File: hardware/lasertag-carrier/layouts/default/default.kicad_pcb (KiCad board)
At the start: 2 copper layers, 75 x 50 mm, 37 parts, among them J0 Power in 2P, J1 S3-Matrix L, J10 LS in, J11 LS out, J12 Ext button, J13 Touch hdr, J2 S3-Matrix R, J3 MAX98357A, J4 Speaker, J5 microSD, J6 IR RX, J7 IR LED, J8 WS2812 out, J9 OLED I2C, Q1 2N2222A, SW1 SW_PUSH_6mm, U1 74AHCT125

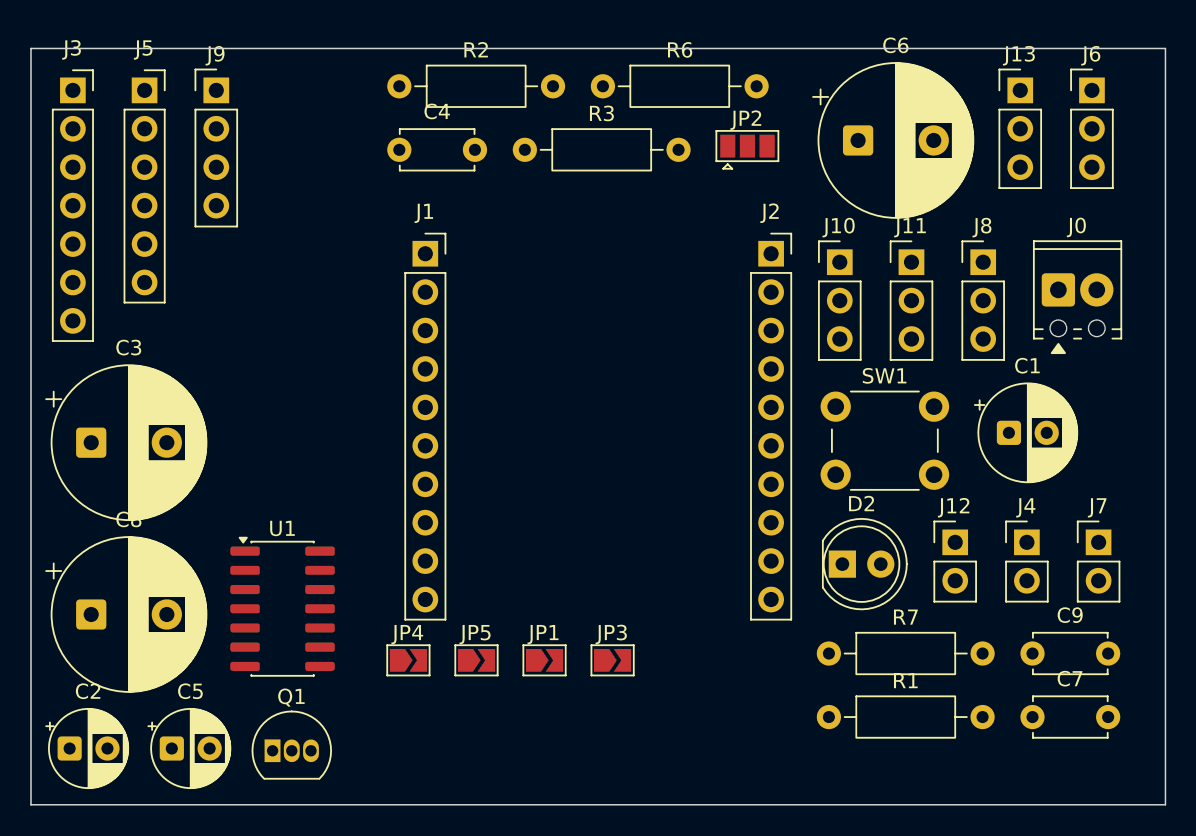
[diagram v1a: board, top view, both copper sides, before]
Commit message: Directed placement; drop level shifter from carrier; add activity-LED header
Floor plan per review: power (J0/C1/D2) bottom-left, audio (J3/C3/JP1/JP2/J4)
mid-left with the MAX98357A body reaching the left edge, microSD (J5/C4/C5/
JP3) bottom-right with the breakout body reaching the right edge, IR RX (J6/
C9) top-centre, IR TX driver (J7/Q1/R1/R2) top-right, GP2 role selector
bottom-centre, WS2812 out (J8/R3/C6) right edge.

- remove the 6 level-shifter parts (J10/J11/U1/R6/C7/C8) from the carrier:
  Block 7 is a standalone board per pcb-blocks.md; the ws-out header J8 stays
  as the cable output that will feed it if ring/status LEDs are added later
- add the activity-LED circuit the spec had deferred (Assumption #9): J14
  2-pin header at 25% from the left on the top edge + R9 220R series, wired
  GP7 (J1.4) -> R9 -> J14 -> GND to match the breadboard circuit the firmware
  already drives (activityLedPin = 7)
- keep main.ato in sync (documentation only -- do not rebuild with ato, the
  board file is the source of truth downstream of the keep-THT decision)
- regenerate bom.csv (33 parts)

Verified: no overlapping bounding boxes, nothing inside the module footprint
or under the elevated audio/microSD breakout bodies, zero DRC errors
(67 unconnected = ratsnest to route, plus cosmetic silk warnings).

Co-Authored-By: Claude Opus 4.8 <noreply@anthropic.com>
Claude-Session: https://claude.ai/code/session_01TutNLcDSScdeeVSbjpyg8j
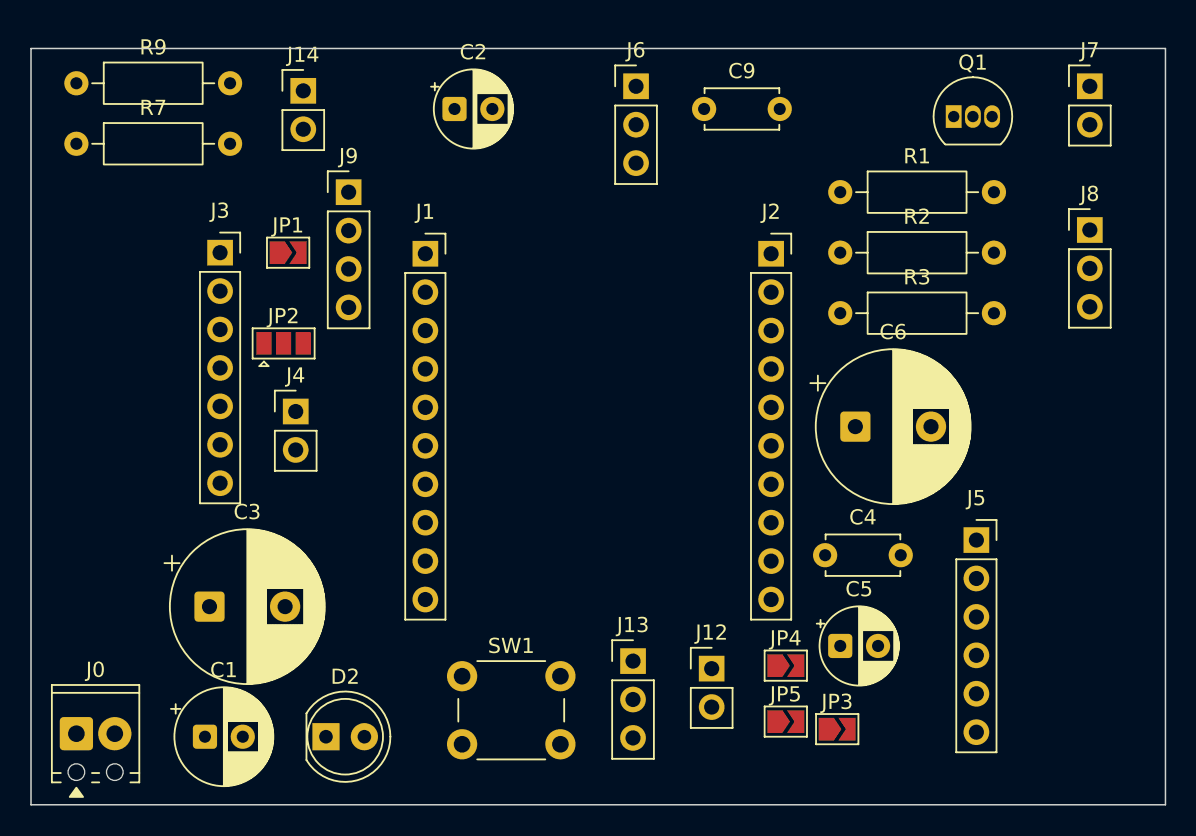
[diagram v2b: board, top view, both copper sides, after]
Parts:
- removed C7: 100nF, Capacitor_THT:C_Disc_D4.7mm_W2.5mm_P5.00mm
- removed C8: 1000uF/10V, Capacitor_THT:CP_Radial_D10.0mm_P5.00mm
- removed J10: LS in, Connector_PinHeader_2.54mm:PinHeader_1x03_P2.54mm_Vertical
- removed J11: LS out, Connector_PinHeader_2.54mm:PinHeader_1x03_P2.54mm_Vertical
- removed R6: 220R, Resistor_THT:R_Axial_DIN0207_L6.3mm_D2.5mm_P10.16mm_Horizontal
- removed U1: 74AHCT125, Package_SO:SOIC-14_3.9x8.7mm_P1.27mm
- added J14: Activity LED, Connector_PinHeader_2.54mm:PinHeader_1x02_P2.54mm_Vertical, F.Cu at (118.0, 62.8)
- added R9: 220R, Resistor_THT:R_Axial_DIN0207_L6.3mm_D2.5mm_P10.16mm_Horizontal, F.Cu at (103.0, 62.3)
- moved J0 71.2 mm to (103.0, 105.3)
- moved J5 62.5 mm to (162.5, 92.5)
- moved Q1 61.5 mm to (161.0, 64.5)
- moved R7 60.1 mm to (103.0, 66.3)
- moved C1 56.8 mm to (111.5, 105.5)
- moved C2 49.3 mm to (128.0, 64.0)
- moved J4 49.1 mm to (117.5, 84.0)
- moved J13 45.6 mm to (139.8, 100.5)
- moved C5 44.7 mm to (153.5, 99.5)
- moved C9 42.0 mm to (144.5, 64.0)
- moved C4 38.9 mm to (152.5, 93.5)
- moved D2 36.0 mm to (119.5, 105.5)
- moved R1 34.7 mm to (153.5, 69.5)
- moved JP2 33.3 mm to (116.7, 79.5)
- moved JP1 31.8 mm to (117.0, 73.5)
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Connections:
- J1 pad 4: _4 -> ACT_LED

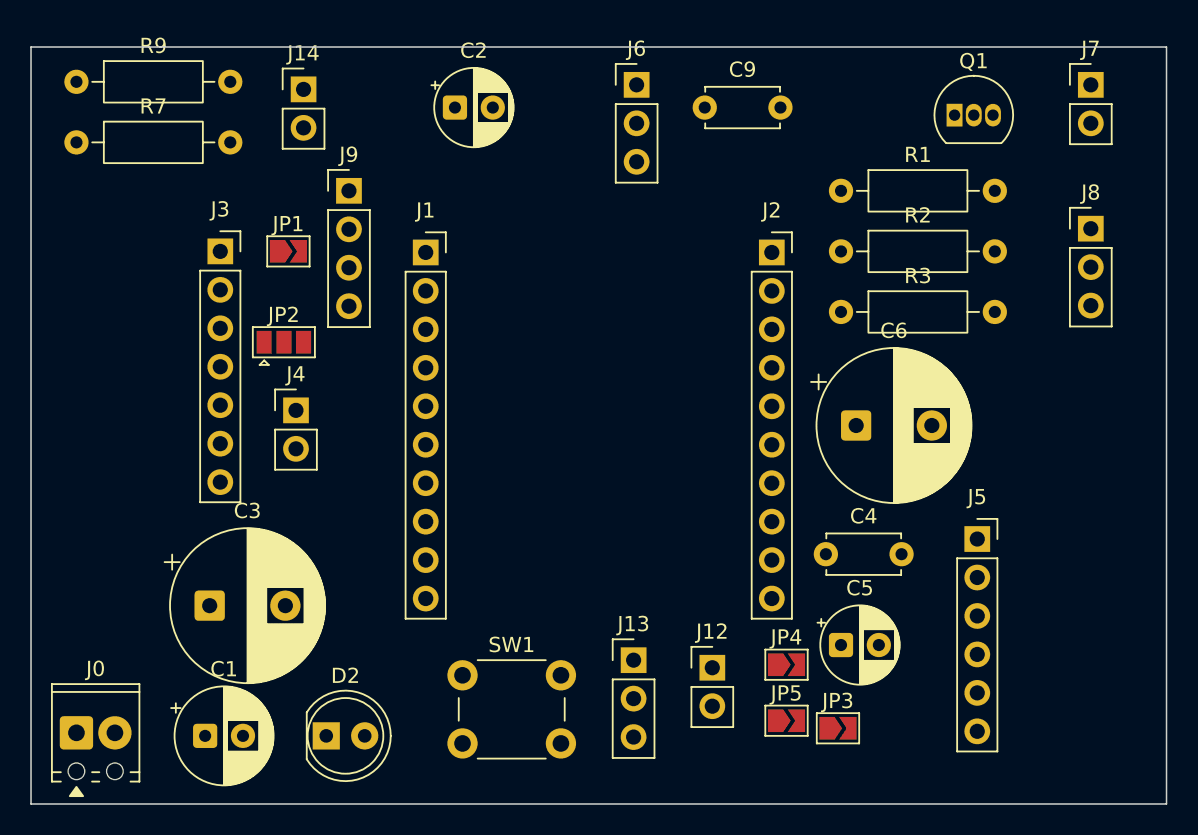
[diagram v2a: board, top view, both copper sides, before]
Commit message: Route the carrier board (Freerouting) with B.Cu GND pour
Pipeline: pcbnew DSN export -> Freerouting 2.1.0 headless (GND as traces,
5 passes, 0 unrouted) -> SES import -> full-board GND pour on B.Cu (solid
pad connections) -> power nets widened to 0.5mm with an iterative DRC guard
that narrows pinch-point segments back to 0.25mm (prevents the widen step
introducing clearance/short violations).

Result: 268 track segments (63 at 0.5mm), 4 vias, all 67 ratsnest
connections routed. DRC: 0 shorts, 0 clearance, 0 unconnected, 0 starved
thermals. Remaining warnings are by-design solder-jumper mask apertures
(JP2/JP4) and cosmetic silkscreen overlaps.

Rotation review: J0 wire entry already faces the bottom edge; Q1 E-B-C order
suits R1 (base, left) and J7 (collector load, right); J1/J2 pin-1 both at the
top matching the module's row order; socket bodies face their board edges.
No rotations needed.

Co-Authored-By: Claude Opus 4.8 <noreply@anthropic.com>
Claude-Session: https://claude.ai/code/session_01TutNLcDSScdeeVSbjpyg8j
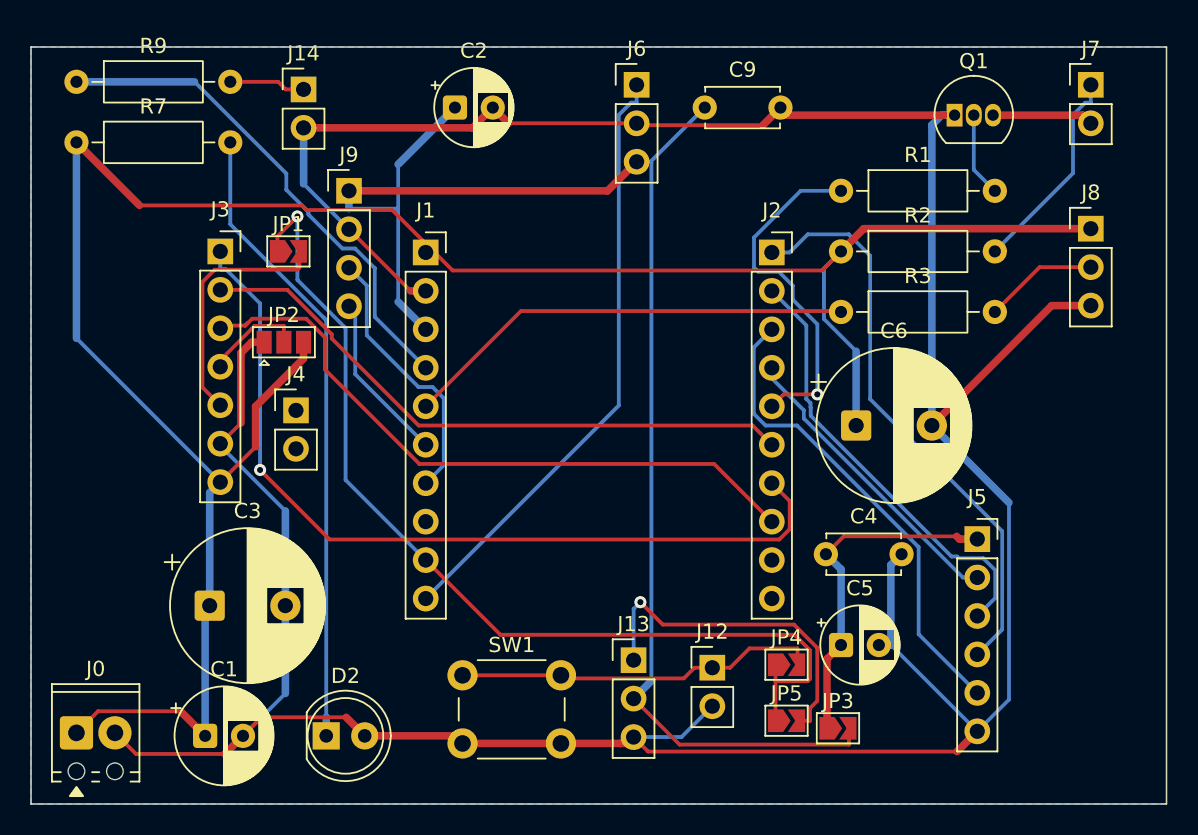
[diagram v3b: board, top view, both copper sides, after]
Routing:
- net GND: track 0.00 -> 230.2 mm
- net VCC5: track 0.00 -> 149.9 mm
- net VCC3V3: track 0.00 -> 99.7 mm
- net audio-a: track 0.00 -> 64.9 mm, vias 0 -> 1
- net i2s_ws: track 0.00 -> 56.4 mm, vias 0 -> 1
- net i2s_din: track 0.00 -> 43.7 mm
- net anode: track 0.00 -> 42.1 mm
- net i2s_bclk: track 0.00 -> 40.8 mm
- net ir_rx: track 0.00 -> 39.9 mm
- net sd_sck: track 0.00 -> 38.2 mm
- net ACT_LED: track 0.00 -> 33.5 mm
- net sd_miso: track 0.00 -> 31.8 mm
- net ws_data: track 0.00 -> 30.1 mm
- net sd_mosi: track 0.00 -> 29.2 mm
- net footprint-a: track 0.00 -> 24.1 mm
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- added copper zone on B.Cu, net GND

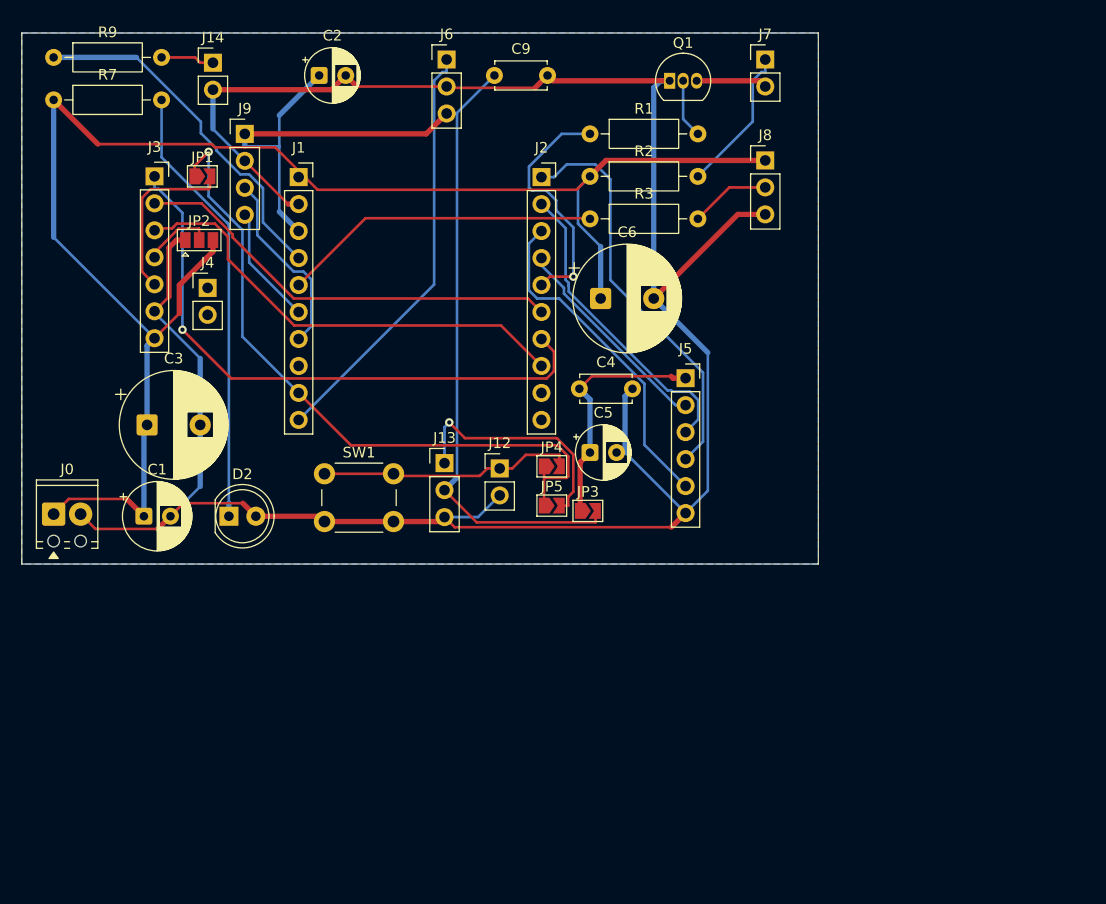
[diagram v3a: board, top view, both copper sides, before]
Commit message: Grow carrier to 100x80mm; add power switch, always-on bridge, M3 holes
Same cheap-fab price tier (<=100x100mm), 2.1x the area: density drops from
~41% to ~19%, which eliminated every silkscreen overlap (7 -> 0) and gives
comfortable hand-soldering access throughout.

- SW2 (SW_DIP_SPSTx01_Slide) in series with the 5V input: J0.1 -> VCC5_IN ->
  SW2 -> VCC5; JP6 solder jumper bridges SW2 for always-on operation
- H1-H4 M3 mounting holes (3.2mm) inset 4.5mm in each corner
- same floor plan, respaced: power+switch bottom-left, audio mid-left (body
  to left edge), microSD bottom-right (body to right edge), IR RX top-centre,
  activity LED at 25% top, IR TX top-right, GP2 selector bottom-centre
- rerouted with Freerouting (0 unrouted), B.Cu GND pour, power nets 0.5mm
  with the iterative narrow-at-pinch-points DRC guard

DRC: 0 shorts, 0 clearance, 0 unconnected, 0 starved thermals, 0 silk
overlaps. Remaining warnings: by-design jumper mask apertures and 4 silk-
near-edge cosmetics (mounting-hole rings, two top-edge refdes).

Co-Authored-By: Claude Opus 4.8 <noreply@anthropic.com>
Claude-Session: https://claude.ai/code/session_01TutNLcDSScdeeVSbjpyg8j
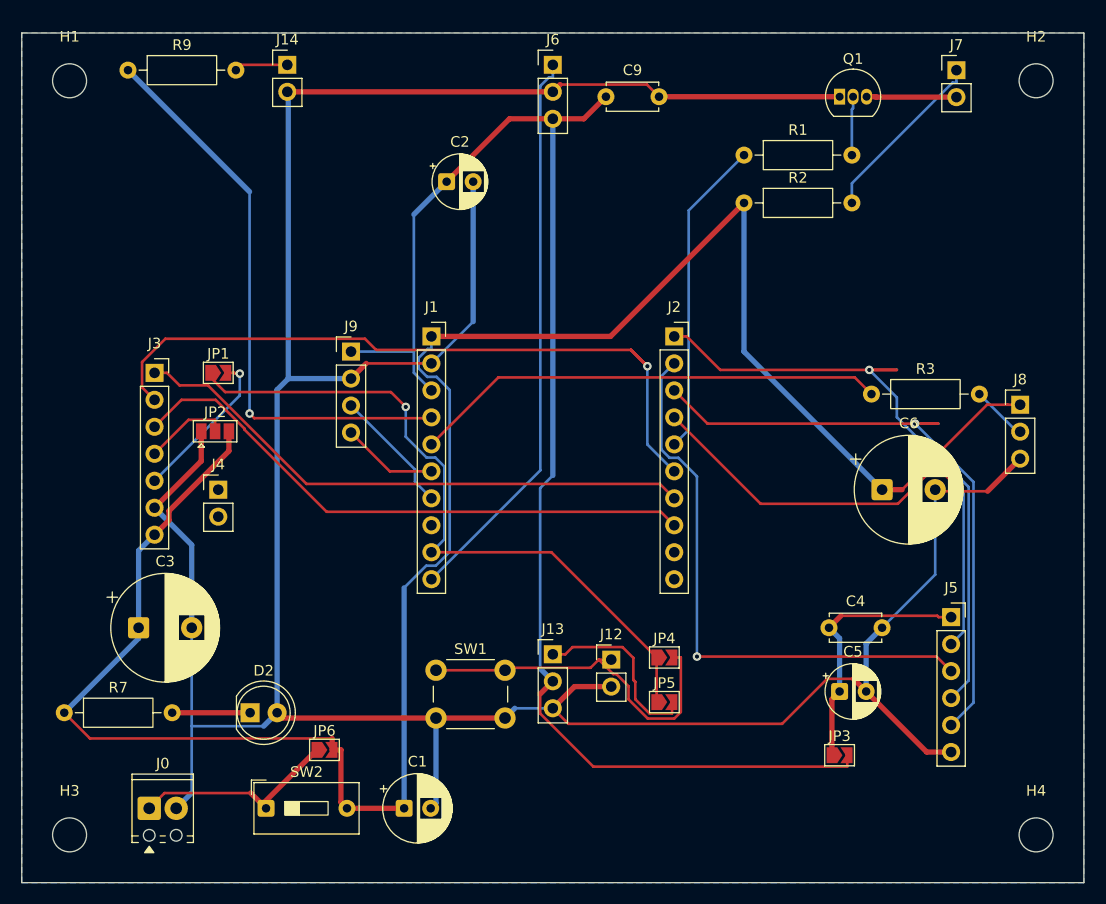
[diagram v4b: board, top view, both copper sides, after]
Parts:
- added H1: M3, MountingHole_3.2mm_M3, F.Cu at (104.5, 64.5)
- added H2: M3, MountingHole_3.2mm_M3, F.Cu at (195.5, 64.5)
- added H3: M3, MountingHole_3.2mm_M3, F.Cu at (104.5, 135.5)
- added H4: M3, MountingHole_3.2mm_M3, F.Cu at (195.5, 135.5)
- added JP6: always-on, SolderJumper-2, F.Cu at (128.5, 127.5)
- added SW2: PWR switch, SW_DIP_SPSTx01_Slide_9.78x4.72mm_W7.62mm_P2.54mm, F.Cu at (123.0, 133.0)
- moved R7 57.7 mm to (104.0, 124.0)
- moved C1 36.8 mm to (136.0, 133.0)
- moved J5 33.6 mm to (187.5, 115.0)
- moved J8 33.2 mm to (194.0, 95.0)
- moved JP3 33.0 mm to (177.0, 128.0)
- moved C4 32.5 mm to (176.0, 116.0)
- moved C5 32.5 mm to (177.0, 122.0)
- moved C6 32.0 mm to (181.0, 103.0)
- moved R3 31.2 mm to (180.0, 94.0)
- moved J0 29.1 mm to (112.0, 133.0)
- moved J9 22.8 mm to (131.0, 90.0)
- moved JP5 21.3 mm to (160.5, 123.0)
- moved SW1 21.3 mm to (139.0, 120.0)
- moved JP4 20.9 mm to (160.5, 118.8)
- moved J12 20.8 mm to (155.5, 119.0)
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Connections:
- J0 pad 1: VCC5 -> VCC5_IN
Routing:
- net GND: track 230.2 -> 307.8 mm
- net VCC5: track 149.9 -> 204.7 mm
- net VCC3V3: track 99.7 -> 135.4 mm
- net anode: track 42.1 -> 7.34 mm
- net i2s_bclk: track 40.8 -> 73.2 mm, vias 0 -> 1
- net sd_miso: track 31.8 -> 64.2 mm, vias 0 -> 1
- net sd_sck: track 38.2 -> 65.6 mm, vias 0 -> 1
- net sd_cs: track 20.0 -> 47.1 mm, vias 0 -> 1
- net sd_mosi: track 29.2 -> 54.5 mm, vias 0 -> 1
- net ACT_LED: track 33.5 -> 54.4 mm, vias 0 -> 1
- net VCC5_IN: track 0.00 -> 19.5 mm
- net ws_data: track 30.1 -> 44.7 mm
- net ir_rx: track 39.9 -> 53.4 mm
- net i2s_din: track 43.7 -> 54.9 mm
- net footprint-a: track 24.1 -> 33.9 mm
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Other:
- board size 75 x 50 mm -> 100 x 80 mm
